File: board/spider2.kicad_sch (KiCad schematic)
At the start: 106 parts, among them J1 NRJ6HH, J10 PJ-320A, J11 PJ359, J12 PJ359, J13 PJ359, J14 PJ359, J15 PJ359, J16 PJ359, J17 A, J19 PJ359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

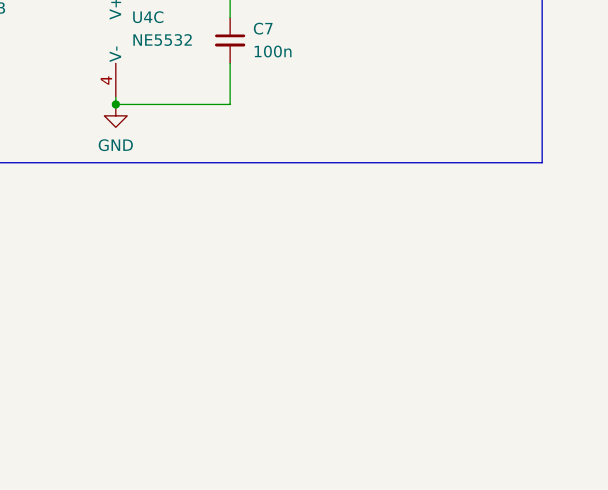
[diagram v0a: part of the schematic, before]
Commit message: option for poti inversion and some missing connections
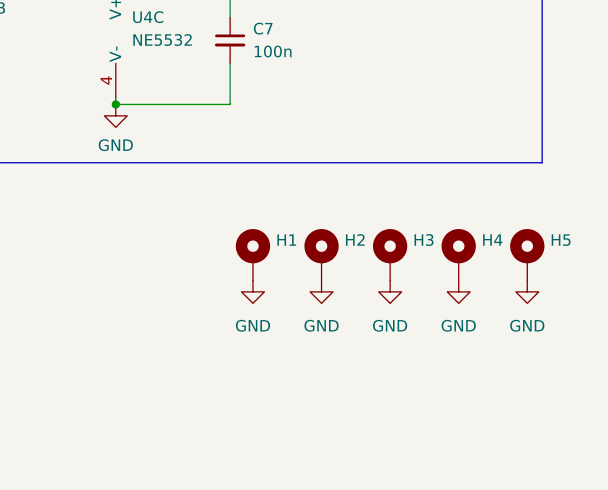
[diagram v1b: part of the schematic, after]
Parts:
- added H1, H2, H3, H4, H5: ~, MountingHole:MountingHole_3.2mm_M3_Pad_Via, symbol Mechanical:MountingHole_Pad
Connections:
- net GND: now also H1.1, H2.1, H3.1, H4.1, H5.1

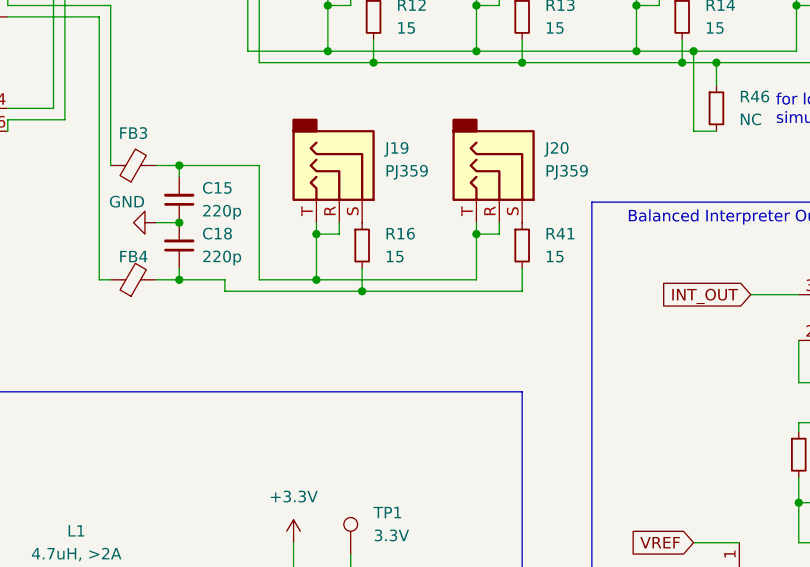
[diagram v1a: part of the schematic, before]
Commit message: hybrid footprints for 3.5mm jacks
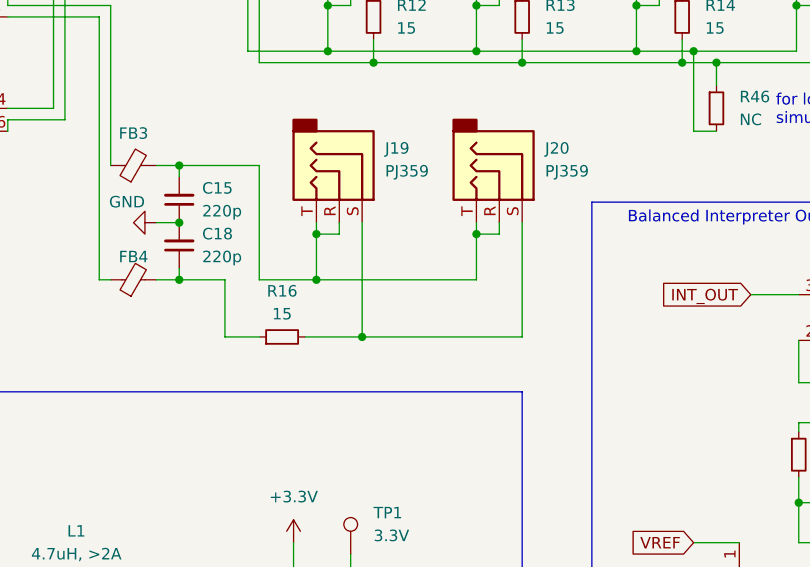
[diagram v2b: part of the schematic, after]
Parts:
- removed R41: 15, Resistor_THT:R_Axial_DIN0207_L6.3mm_D2.5mm_P10.16mm_Horizontal, symbol Device:R_Small
- J11, J12, J13, J14, J15, J16, J19, J20, J3, J4, J5, J7, J8, J9: footprint custom:Jack_3.5mm_PJ359 -> custom:Jack_3.5mm_Hybrid_PJ359_20-1655
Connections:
- net at C18.1, FB4.2: now also R16.1; no longer R16.2
- net at J20.S: now also J19.S, R16.2
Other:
- moved on the sheet: R16
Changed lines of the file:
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@@
 	)
 	(junction
+		(at 158.75 107.95)
+		(diameter 0)
+		(color 0 0 0 0)
+	)
+	(junction
 		(at 171.45 54.61)
 		(diameter 0)
@@
 	)
 	(junction
-		(at 158.75 102.87)
-		(diameter 0)
-		(color 0 0 0 0)
-	)
-	(junction
 		(at 116.84 38.1)
 		(diameter 0)
@@
 	(wire
 		(pts
+			(xy 152.4 107.95) (xy 158.75 107.95)
+		)
+		(stroke
+			(width 0)
+			(type default)
+		)
+	)
+	(wire
+		(pts
 			(xy 124.46 82.55) (xy 124.46 46.99)
 		)
@@
 	(wire
 		(pts
+			(xy 158.75 107.95) (xy 158.75 95.25)
+		)
+		(stroke
+			(width 0)
+			(type default)
+		)
+	)
+	(wire
+		(pts
 			(xy 53.34 137.16) (xy 55.88 137.16)
 		)
@@
 	(wire
 		(pts
-			(xy 143.51 102.87) (xy 158.75 102.87)
-		)
-		(stroke
-			(width 0)
-			(type default)
-		)
-	)
-	(wire
-		(pts
 			(xy 226.06 105.791) (xy 222.504 105.791)
 		)
@@
 	(wire
 		(pts
-			(xy 236.22 42.926) (xy 236.22 36.83)
+			(xy 143.51 107.95) (xy 147.32 107.95)
 		)
 		(stroke
@@
 	(wire
 		(pts
-			(xy 256.54 116.84) (xy 256.54 115.57)
+			(xy 236.22 42.926) (xy 236.22 36.83)
 		)
 		(stroke
@@
 	(wire
 		(pts
-			(xy 154.94 33.02) (xy 171.45 33.02)
+			(xy 256.54 116.84) (xy 256.54 115.57)
 		)
 		(stroke
@@
 	(wire
 		(pts
-			(xy 209.55 71.12) (xy 209.55 69.85)
+			(xy 154.94 33.02) (xy 171.45 33.02)
 		)
 		(stroke
@@
 	(wire
 		(pts
-			(xy 157.48 186.69) (xy 157.48 184.15)
+			(xy 209.55 71.12) (xy 209.55 69.85)
 		)
 		(stroke
@@
 	(wire
 		(pts
-			(xy 53.34 152.4) (xy 53.34 137.16)
+			(xy 157.48 186.69) (xy 157.48 184.15)
 		)
 		(stroke
@@
 	(wire
 		(pts
-			(xy 146.05 76.2) (xy 154.94 76.2)
+			(xy 53.34 152.4) (xy 53.34 137.16)
 		)
 		(stroke
@@
 	(wire
 		(pts
-			(xy 270.51 50.8) (xy 270.51 52.07)
+			(xy 146.05 76.2) (xy 154.94 76.2)
 		)
 		(stroke
@@
 	(wire
 		(pts
-			(xy 158.75 102.87) (xy 158.75 100.33)
+			(xy 270.51 50.8) (xy 270.51 52.07)
 		)
 		(stroke
@@
 	(wire
 		(pts
+			(xy 176.53 95.25) (xy 176.53 107.95)
+		)
+		(stroke
+			(width 0)
+			(type default)
+		)
+	)
+	(wire
+		(pts
 			(xy 171.45 49.53) (xy 173.99 49.53)
 		)
@@
 	(wire
 		(pts
+			(xy 176.53 107.95) (xy 158.75 107.95)
+		)
+		(stroke
+			(width 0)
+			(type default)
+		)
+	)
+	(wire
+		(pts
 			(xy 147.32 55.88) (xy 147.32 34.29)
 		)
@@
 	(wire
 		(pts
-			(xy 176.53 102.87) (xy 176.53 100.33)
-		)
-		(stroke
-			(width 0)
-			(type default)
-		)
-	)
-	(wire
-		(pts
-			(xy 143.51 101.6) (xy 143.51 102.87)
+			(xy 143.51 101.6) (xy 143.51 107.95)
 		)
 		(stroke
@@
 	(wire
 		(pts
-			(xy 158.75 102.87) (xy 176.53 102.87)
-		)
-		(stroke
-			(width 0)
-			(type default)
-		)
-	)
-	(wire
-		(pts
 			(xy 119.38 72.39) (xy 129.54 72.39)
 		)
@@
 			)
 		)
-		(property "Footprint" "custom:Jack_3.5mm_PJ359"
+		(property "Footprint" "custom:Jack_3.5mm_Hybrid_PJ359_20-1655"
 			(at 157.48 64.77 0)
 			(effects
@@
 			)
 		)
-		(property "Footprint" "custom:Jack_3.5mm_PJ359"
+		(property "Footprint" "custom:Jack_3.5mm_Hybrid_PJ359_20-1655"
 			(at 157.48 21.59 0)
 			(effects
@@
 			)
 		)
-		(property "Footprint" "custom:Jack_3.5mm_PJ359"
+		(property "Footprint" "custom:Jack_3.5mm_Hybrid_PJ359_20-1655"
 			(at 209.55 21.59 0)
 			(effects
@@
 			)
 		)
-		(property "Footprint" "custom:Jack_3.5mm_PJ359"
+		(property "Footprint" "custom:Jack_3.5mm_Hybrid_PJ359_20-1655"
 			(at 191.77 64.77 0)
 			(effects
@@
 	)
 	(symbol
-		(lib_id "Device:R_Small")
-		(at 176.53 97.79 0)
-		(unit 1)
-		(exclude_from_sim no)
-		(in_bom yes)
-		(on_board yes)
-		(dnp no)
-		(fields_autoplaced yes)
-		(property "Reference" "R41"
-			(at 179.07 96.5199 0)
-			(effects
-				(font
-					(size 1.27 1.27)
-				)
-				(justify left)
-			)
-		)
-		(property "Value" "15"
-			(at 179.07 99.0599 0)
-			(effects
-				(font
-					(size 1.27 1.27)
-				)
-				(justify left)
-			)
-		)
-		(property "Footprint" "Resistor_THT:R_Axial_DIN0207_L6.3mm_D2.5mm_P10.16mm_Horizontal"
-			(at 176.53 97.79 0)
-			(effects
-				(font
-					(size 1.27 1.27)
-				)
-				(hide yes)
-			)
-		)
-		(property "Datasheet" "~"
-			(at 176.53 97.79 0)
-			(effects
-				(font
-					(size 1.27 1.27)
-				)
-				(hide yes)
-			)
-		)
-		(property "Description" "Resistor, small symbol"
-			(at 176.53 97.79 0)
-			(effects
-				(font
-					(size 1.27 1.27)
-				)
-				(hide yes)
-			)
-		)
-		(property "Sim.Device" ""
-			(at 176.53 97.79 0)
-			(effects
-				(font
-					(size 1.27 1.27)
-				)
-				(hide yes)
-			)
-		)
-		(property "Sim.Pins" ""
-			(at 176.53 97.79 0)
-			(effects
-				(font
-					(size 1.27 1.27)
-				)
-				(hide yes)
-			)
-		)
-		(property "Sim.Type" ""
-			(at 176.53 97.79 0)
-			(effects
-				(font
-					(size 1.27 1.27)
-				)
-				(hide yes)
-			)
-		)
-		(pin "2"
-		)
-		(pin "1"
-		)
-		(instances
-			(project "spider2"
-				(path "/31073f88-a990-4ecc-8ab9-bb6b56c98e1e"
-					(reference "R41")
-					(unit 1)
-				)
-			)
-		)
-	)
-	(symbol
 		(lib_id "Connector:TestPoint")
 		(at 60.96 82.55 0)
@@
 			)
 		)
-		(property "Footprint" "custom:Jack_3.5mm_PJ359"
+		(property "Footprint" "custom:Jack_3.5mm_Hybrid_PJ359_20-1655"
 			(at 156.21 90.17 0)
 			(effects
@@
 			)
 		)
-		(property "Footprint" "custom:Jack_3.5mm_PJ359"
+		(property "Footprint" "custom:Jack_3.5mm_Hybrid_PJ359_20-1655"
 			(at 191.77 43.18 0)
 			(effects
@@
 	(symbol
 		(lib_id "Device:R_Small")
-		(at 158.75 97.79 0)
+		(at 149.86 107.95 90)
 		(unit 1)
 		(exclude_from_sim no)
@@
 		(fields_autoplaced yes)
 		(property "Reference" "R16"
-			(at 161.29 96.5199 0)
+			(at 149.86 102.87 90)
 			(effects
 				(font
 					(size 1.27 1.27)
 				)
-				(justify left)
 			)
 		)
 		(property "Value" "15"
-			(at 161.29 99.0599 0)
+			(at 149.86 105.41 90)
 			(effects
 				(font
 					(size 1.27 1.27)
 				)
-				(justify left)
 			)
 		)
 		(property "Footprint" "Resistor_THT:R_Axial_DIN0207_L6.3mm_D2.5mm_P10.16mm_Horizontal"
-			(at 158.75 97.79 0)
+			(at 149.86 107.95 0)
 			(effects
 				(font
@@
 		)
 		(property "Datasheet" "~"
-			(at 158.75 97.79 0)
+			(at 149.86 107.95 0)
 			(effects
 				(font
@@
 		)
 		(property "Description" "Resistor, small symbol"
-			(at 158.75 97.79 0)
+			(at 149.86 107.95 0)
 			(effects
 				(font
@@
 		)
 		(property "Sim.Device" ""
-			(at 158.75 97.79 0)
+			(at 149.86 107.95 0)
 			(effects
 				(font
@@
 		)
 		(property "Sim.Pins" ""
-			(at 158.75 97.79 0)
+			(at 149.86 107.95 0)
 			(effects
 				(font
@@
 		)
 		(property "Sim.Type" ""
-			(at 158.75 97.79 0)
+			(at 149.86 107.95 0)
 			(effects
 				(font
@@
 			)
 		)
-		(property "Footprint" "custom:Jack_3.5mm_PJ359"
+		(property "Footprint" "custom:Jack_3.5mm_Hybrid_PJ359_20-1655"
 			(at 173.99 21.59 0)
 			(effects
@@
 			)
 		)
-		(property "Footprint" "custom:Jack_3.5mm_PJ359"
+		(property "Footprint" "custom:Jack_3.5mm_Hybrid_PJ359_20-1655"
 			(at 209.55 64.77 0)
 			(effects
@@
 			)
 		)
-		(property "Footprint" "custom:Jack_3.5mm_PJ359"
+		(property "Footprint" "custom:Jack_3.5mm_Hybrid_PJ359_20-1655"
 			(at 173.99 90.17 0)
 			(effects
@@
 			)
 		)
-		(property "Footprint" "custom:Jack_3.5mm_PJ359"
+		(property "Footprint" "custom:Jack_3.5mm_Hybrid_PJ359_20-1655"
 			(at 209.55 43.18 0)
 			(effects
@@
 			)
 		)
-		(property "Footprint" "custom:Jack_3.5mm_PJ359"
+		(property "Footprint" "custom:Jack_3.5mm_Hybrid_PJ359_20-1655"
 			(at 173.99 43.18 0)
 			(effects
@@
 			)
 		)
-		(property "Footprint" "custom:Jack_3.5mm_PJ359"
+		(property "Footprint" "custom:Jack_3.5mm_Hybrid_PJ359_20-1655"
 			(at 191.77 21.59 0)
 			(effects
@@
 			)
 		)
-		(property "Footprint" "custom:Jack_3.5mm_PJ359"
+		(property "Footprint" "custom:Jack_3.5mm_Hybrid_PJ359_20-1655"
 			(at 157.48 43.18 0)
 			(effects
@@
 			)
 		)
-		(property "Footprint" "custom:Jack_3.5mm_PJ359"
+		(property "Footprint" "custom:Jack_3.5mm_Hybrid_PJ359_20-1655"
 			(at 173.99 64.77 0)
 			(effects

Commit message: some cleanups
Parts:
- C17, C26, C29, C30, C33, C35, C36, L2, R43, R44, R46: now not fitted; now left out of the parts list
- J17, JP5, TP1, TP2, TP3, TP4, TP5, TP6, TP7: now left out of the parts list
- U7: Mouser (none) -> https://eu.mouser.com/ProductDetail/621-PAM8406DR
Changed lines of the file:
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@@
 		(unit 1)
 		(exclude_from_sim no)
-		(in_bom yes)
+		(in_bom no)
 		(on_board yes)
-		(dnp no)
+		(dnp yes)
 		(fields_autoplaced yes)
 		(property "Reference" "R46"
@@
 			)
 		)
-		(property "Datasheet" "~"
+		(property "Datasheet" "https://eu.mouser.com/datasheet/2/140/200-3304369.pdf"
 			(at 36.83 125.73 0)
 			(effects
@@
 		(unit 1)
 		(exclude_from_sim no)
-		(in_bom yes)
+		(in_bom no)
 		(on_board yes)
-		(dnp no)
+		(dnp yes)
 		(fields_autoplaced yes)
 		(property "Reference" "R43"
@@
 		(unit 1)
 		(exclude_from_sim no)
-		(in_bom yes)
+		(in_bom no)
 		(on_board yes)
 		(dnp no)
@@
 		(unit 1)
 		(exclude_from_sim no)
-		(in_bom yes)
+		(in_bom no)
 		(on_board yes)
 		(dnp no)
@@
 		(unit 1)
 		(exclude_from_sim no)
-		(in_bom yes)
+		(in_bom no)
 		(on_board yes)
 		(dnp no)
@@
 			)
 		)
-		(property "Datasheet" "~"
+		(property "Datasheet" "https://wmsc.lcsc.com/wmsc/upload/file/pdf/v2/lcsc/2311241628_Hong-Cheng-HC-PJ-320A_C7501806.pdf"
 			(at 262.89 133.35 0)
 			(effects
@@
 		(unit 1)
 		(exclude_from_sim no)
-		(in_bom yes)
+		(in_bom no)
 		(on_board yes)
-		(dnp no)
+		(dnp yes)
 		(fields_autoplaced yes)
 		(property "Reference" "R44"
@@
 		(unit 1)
 		(exclude_from_sim no)
-		(in_bom yes)
+		(in_bom no)
 		(on_board yes)
 		(dnp no)
@@
 		(unit 1)
 		(exclude_from_sim no)
-		(in_bom yes)
+		(in_bom no)
 		(on_board yes)
 		(dnp no)
@@
 			)
 		)
-		(property "Sim.Device" ""
+		(property "Mouser" "https://eu.mouser.com/ProductDetail/621-PAM8406DR"
 			(at 104.14 77.47 0)
 			(effects
@@
 		(unit 1)
 		(exclude_from_sim no)
-		(in_bom yes)
+		(in_bom no)
 		(on_board yes)
 		(dnp no)
@@
 		(unit 1)
 		(exclude_from_sim no)
-		(in_bom yes)
+		(in_bom no)
 		(on_board yes)
 		(dnp no)
@@
 		(unit 1)
 		(exclude_from_sim yes)
-		(in_bom yes)
+		(in_bom no)
 		(on_board yes)
 		(dnp no)
@@
 			)
 		)
-		(property "Datasheet" "~"
+		(property "Datasheet" "https://www.tme.eu/Document/0cc9448b759d8f4845600d6775144bd3/AOI4286.pdf"
 			(at 38.1 138.43 0)
 			(effects
@@
 		(unit 1)
 		(exclude_from_sim no)
-		(in_bom yes)
+		(in_bom no)
 		(on_board yes)
-		(dnp no)
+		(dnp yes)
 		(property "Reference" "C33"
 			(at 99.06 146.05 0)
@@
 		(unit 1)
 		(exclude_from_sim no)
-		(in_bom yes)
+		(in_bom no)
 		(on_board yes)
-		(dnp no)
+		(dnp yes)
 		(property "Reference" "C26"
 			(at 123.698 30.48 0)
@@
 		(unit 1)
 		(exclude_from_sim no)
-		(in_bom yes)
+		(in_bom no)
 		(on_board yes)
-		(dnp no)
+		(dnp yes)
 		(property "Reference" "C29"
 			(at 99.568 30.48 0)
@@
 		(unit 1)
 		(exclude_from_sim no)
-		(in_bom yes)
+		(in_bom no)
 		(on_board yes)
-		(dnp no)
+		(dnp yes)
 		(fields_autoplaced yes)
 		(property "Reference" "L2"
@@
 		(unit 1)
 		(exclude_from_sim no)
-		(in_bom yes)
+		(in_bom no)
 		(on_board yes)
-		(dnp no)
+		(dnp yes)
 		(property "Reference" "C30"
 			(at 116.078 177.8 0)
@@
 			)
 		)
-		(property "Datasheet" "~"
+		(property "Datasheet" "https://wmsc.lcsc.com/wmsc/upload/file/pdf/v2/lcsc/2311241628_Hong-Cheng-HC-PJ-320A_C7501806.pdf"
 			(at 262.89 113.03 0)
 			(effects
@@
 		(unit 1)
 		(exclude_from_sim no)
-		(in_bom yes)
+		(in_bom no)
 		(on_board yes)
-		(dnp no)
+		(dnp yes)
 		(property "Reference" "C36"
 			(at 167.64 139.7 0)
@@
 			)
 		)
-		(property "Datasheet" "~"
+		(property "Datasheet" "https://eu.mouser.com/datasheet/2/140/200-3304369.pdf"
 			(at 60.96 134.62 0)
 			(effects
@@
 		(unit 1)
 		(exclude_from_sim no)
-		(in_bom yes)
+		(in_bom no)
 		(on_board yes)
-		(dnp no)
+		(dnp yes)
 		(property "Reference" "C17"
 			(at 83.058 143.51 0)
@@
 		(unit 1)
 		(exclude_from_sim no)
-		(in_bom yes)
+		(in_bom no)
 		(on_board yes)
 		(dnp no)
@@
 		(unit 1)
 		(exclude_from_sim no)
-		(in_bom yes)
+		(in_bom no)
 		(on_board yes)
-		(dnp no)
+		(dnp yes)
 		(property "Reference" "C35"
 			(at 157.48 139.7 0)
